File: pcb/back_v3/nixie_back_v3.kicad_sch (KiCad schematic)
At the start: 21 parts, among them J1 UART, J2 BUTTONS, J3 LED, J4 POWER, J5 LEFT, J6 RIGHT, SW1 BOOT, SW2 RESET, U1 DS3231MZ, U2 ESP32-WROOM-E

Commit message: Rename kicad project
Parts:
- J5: value LEFT -> CONN_LEFT
- J6: value RIGHT -> CONN_RIGHT
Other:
- company: (none) -> Ilya Strukov
- title: (none) -> Nixie Clock Back Panel

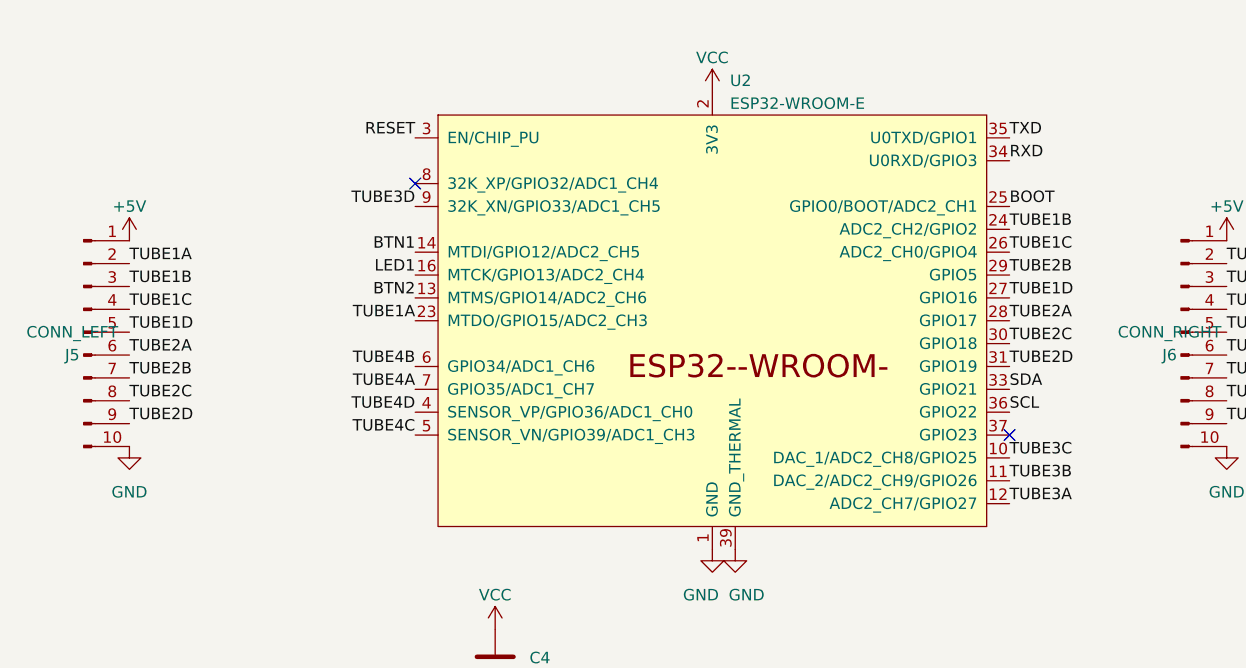
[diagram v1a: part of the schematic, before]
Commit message: Fix pin assignment on v3 back pcb
GPIO pins 34-39 on ESP32 are input only.
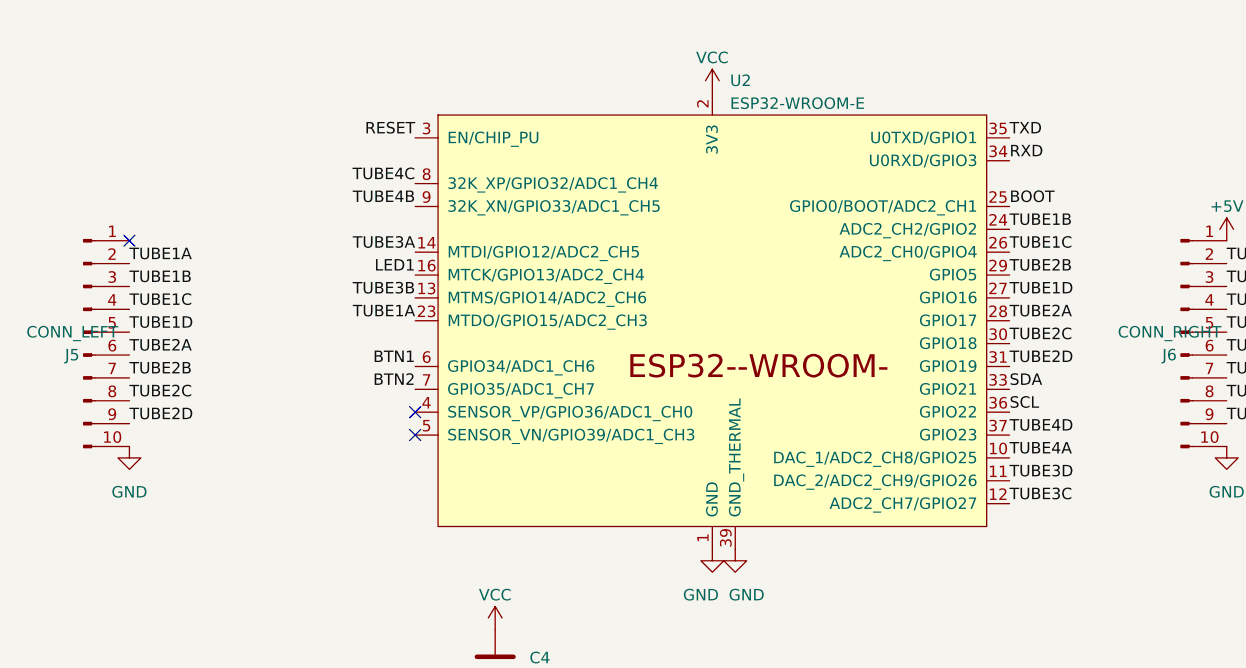
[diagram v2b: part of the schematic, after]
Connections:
- net +5V: no longer J5.1 (Pin_1)
- net BTN1: now also U2.6 (GPIO34/ADC1_CH6); no longer U2.14 (MTDI/GPIO12/ADC2_CH5)
- net BTN2: now also U2.7 (GPIO35/ADC1_CH7); no longer U2.13 (MTMS/GPIO14/ADC2_CH6)
- net TUBE3A: now also U2.14 (MTDI/GPIO12/ADC2_CH5); no longer U2.12 (ADC2_CH7/GPIO27)
- net TUBE3B: now also U2.13 (MTMS/GPIO14/ADC2_CH6); no longer U2.11 (DAC_2/ADC2_CH9/GPIO26)
- net TUBE3C: now also U2.12 (ADC2_CH7/GPIO27); no longer U2.10 (DAC_1/ADC2_CH8/GPIO25)
- net TUBE3D: now also U2.11 (DAC_2/ADC2_CH9/GPIO26); no longer U2.9 (32K_XN/GPIO33/ADC1_CH5)
- net TUBE4A: now also U2.10 (DAC_1/ADC2_CH8/GPIO25); no longer U2.7 (GPIO35/ADC1_CH7)
- net TUBE4B: now also U2.9 (32K_XN/GPIO33/ADC1_CH5); no longer U2.6 (GPIO34/ADC1_CH6)
- net TUBE4C: now also U2.8 (32K_XP/GPIO32/ADC1_CH4); no longer U2.5 (SENSOR_VN/GPIO39/ADC1_CH3)
- net TUBE4D: now also U2.37 (GPIO23); no longer U2.4 (SENSOR_VP/GPIO36/ADC1_CH0)
- no-connect marks 6 -> 7
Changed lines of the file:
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@@
   (title_block
     (title "Nixie Clock Back Panel")
-    (rev "3.0")
+    (rev "3.1")
     (company "Ilya Strukov")
   )
@@
   )
   (no_connect (at 236.22 92.71))
-  (no_connect (at 135.89 123.19))
+  (no_connect (at 69.85 123.19))
+  (no_connect (at 69.85 120.65))
   (no_connect (at 236.22 100.33))
+  (no_connect (at 38.1 101.6))
   (no_connect (at 180.34 41.91))
   (no_connect (at 170.18 41.91))
-  (no_connect (at 69.85 95.25))
   (wire (pts (xy 44.45 46.99) (xy 44.45 43.18))
     (stroke (width 0) (type default))
@@
     (effects (font (size 1.27 1.27)) (justify left bottom))
   )
-  (label "BTN2" (at 69.85 107.95 180) (fields_autoplaced)
+  (label "BTN2" (at 69.85 118.11 180) (fields_autoplaced)
     (effects (font (size 1.27 1.27)) (justify right bottom))
   )
@@
     (effects (font (size 1.27 1.27)) (justify right bottom))
   )
-  (label "TUBE3C" (at 135.89 125.73 0) (fields_autoplaced)
-    (effects (font (size 1.27 1.27)) (justify left bottom))
-  )
-  (label "TUBE3A" (at 135.89 130.81 0) (fields_autoplaced)
-    (effects (font (size 1.27 1.27)) (justify left bottom))
+  (label "TUBE3C" (at 135.89 130.81 0) (fields_autoplaced)
+    (effects (font (size 1.27 1.27)) (justify left bottom))
+  )
+  (label "TUBE3A" (at 69.85 102.87 180) (fields_autoplaced)
+    (effects (font (size 1.27 1.27)) (justify right bottom))
   )
   (label "TUBE3D" (at 160.02 111.76 0) (fields_autoplaced)
@@
     (effects (font (size 1.27 1.27)) (justify left bottom))
   )
-  (label "TUBE3B" (at 135.89 128.27 0) (fields_autoplaced)
-    (effects (font (size 1.27 1.27)) (justify left bottom))
+  (label "TUBE3B" (at 69.85 107.95 180) (fields_autoplaced)
+    (effects (font (size 1.27 1.27)) (justify right bottom))
   )
   (label "TUBE1A" (at 69.85 110.49 180) (fields_autoplaced)
@@
     (effects (font (size 1.27 1.27)) (justify right bottom))
   )
-  (label "TUBE3D" (at 69.85 97.79 180) (fields_autoplaced)
-    (effects (font (size 1.27 1.27)) (justify right bottom))
-  )
-  (label "TUBE4B" (at 69.85 115.57 180) (fields_autoplaced)
+  (label "TUBE3D" (at 135.89 128.27 0) (fields_autoplaced)
+    (effects (font (size 1.27 1.27)) (justify left bottom))
+  )
+  (label "TUBE4B" (at 69.85 97.79 180) (fields_autoplaced)
     (effects (font (size 1.27 1.27)) (justify right bottom))
   )
@@
     (effects (font (size 1.27 1.27)) (justify left bottom))
   )
-  (label "TUBE4A" (at 69.85 118.11 180) (fields_autoplaced)
-    (effects (font (size 1.27 1.27)) (justify right bottom))
+  (label "TUBE4A" (at 135.89 125.73 0) (fields_autoplaced)
+    (effects (font (size 1.27 1.27)) (justify left bottom))
   )
   (label "TUBE1C" (at 38.1 109.22 0) (fields_autoplaced)
@@
     (effects (font (size 1.27 1.27)) (justify left bottom))
   )
-  (label "TUBE4C" (at 69.85 123.19 180) (fields_autoplaced)
+  (label "TUBE4C" (at 69.85 95.25 180) (fields_autoplaced)
     (effects (font (size 1.27 1.27)) (justify right bottom))
   )
@@
     (effects (font (size 1.27 1.27)) (justify left bottom))
   )
-  (label "TUBE4D" (at 69.85 120.65 180) (fields_autoplaced)
-    (effects (font (size 1.27 1.27)) (justify right bottom))
-  )
-  (label "BTN1" (at 69.85 102.87 180) (fields_autoplaced)
+  (label "TUBE4D" (at 135.89 123.19 0) (fields_autoplaced)
+    (effects (font (size 1.27 1.27)) (justify left bottom))
+  )
+  (label "BTN1" (at 69.85 115.57 180) (fields_autoplaced)
     (effects (font (size 1.27 1.27)) (justify right bottom))
   )
@@
         )
       )
-    )
-  )
-  (symbol (lib_id "power:+5V") (at 38.1 101.6 0) (unit 1)
-    (in_bom yes) (on_board yes) (dnp no) (fields_autoplaced)
-    (property "Reference" "#PWR022" (at 38.1 105.41 0)
-      (effects (font (size 1.27 1.27)) hide)
-    )
-    (property "Value" "+5V" (at 38.1 97.79 0)
-      (effects (font (size 1.27 1.27)))
-    )
-    (property "Footprint" "" (at 38.1 101.6 0)
-      (effects (font (size 1.27 1.27)) hide)
-    )
-    (property "Datasheet" "" (at 38.1 101.6 0)
-      (effects (font (size 1.27 1.27)) hide)
-    )
-    (pin "1")
-    (instances
-      (project "nixie_back_v3"
-        (path "/5f5f2a04-934c-41e7-a231-3b002410944f"
-          (reference "#PWR022") (unit 1)
-        )
-      )
